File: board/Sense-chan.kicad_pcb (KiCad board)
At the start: 2 copper layers, 60 x 46 mm, 49 parts, among them J1 B3B-EH-A, J2 LCD Flexible Cable, J3 DF40HC(3.0)-100DS-0.4V, J4 DM3AT, J5 B4B-EH-A, J6 B4B-EH-A, J7 B3B-EH-A, J8 PinHeader 2.0mm, J9 PinHeader 2.0mm, Q1 IRFML8244TRPBF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

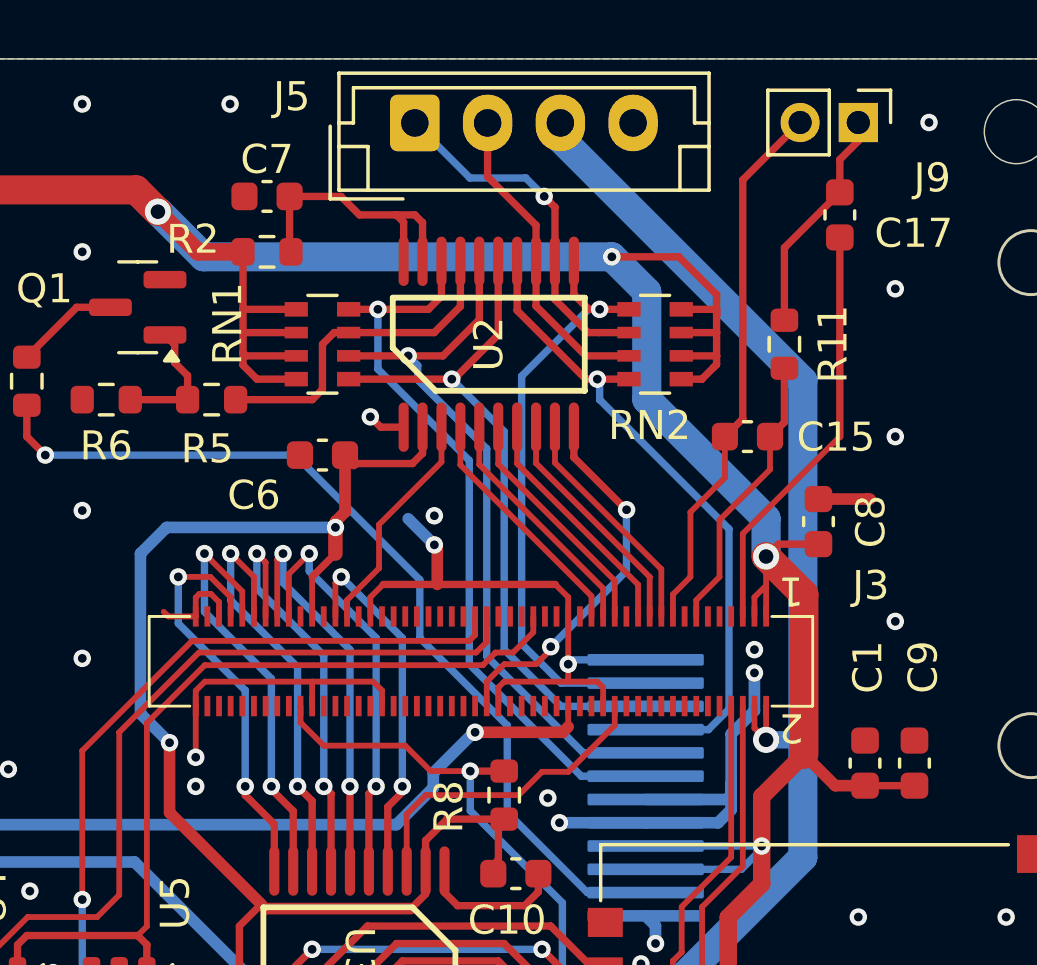
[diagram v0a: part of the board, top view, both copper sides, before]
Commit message: add teardrops to PCB pattern
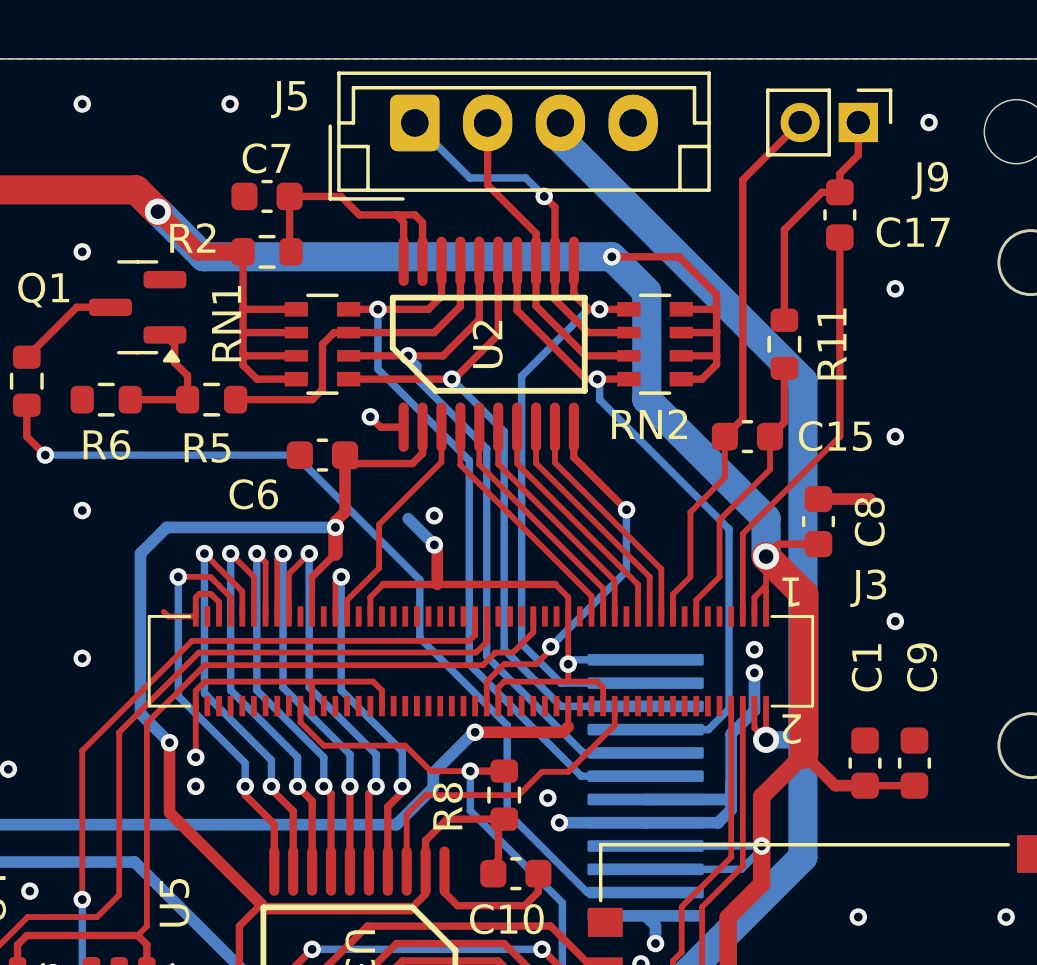
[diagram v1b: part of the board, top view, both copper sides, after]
